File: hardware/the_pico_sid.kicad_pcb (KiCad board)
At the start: 4 copper layers, 26.7 x 56.5 mm, 22 parts, among them J2 Conn_01x05, Q1 2N7002, Q2 2N7002, U1 LM324, U2 SID_6581, U3 Pico, U4 4050, U5 4050, U6 74HC245

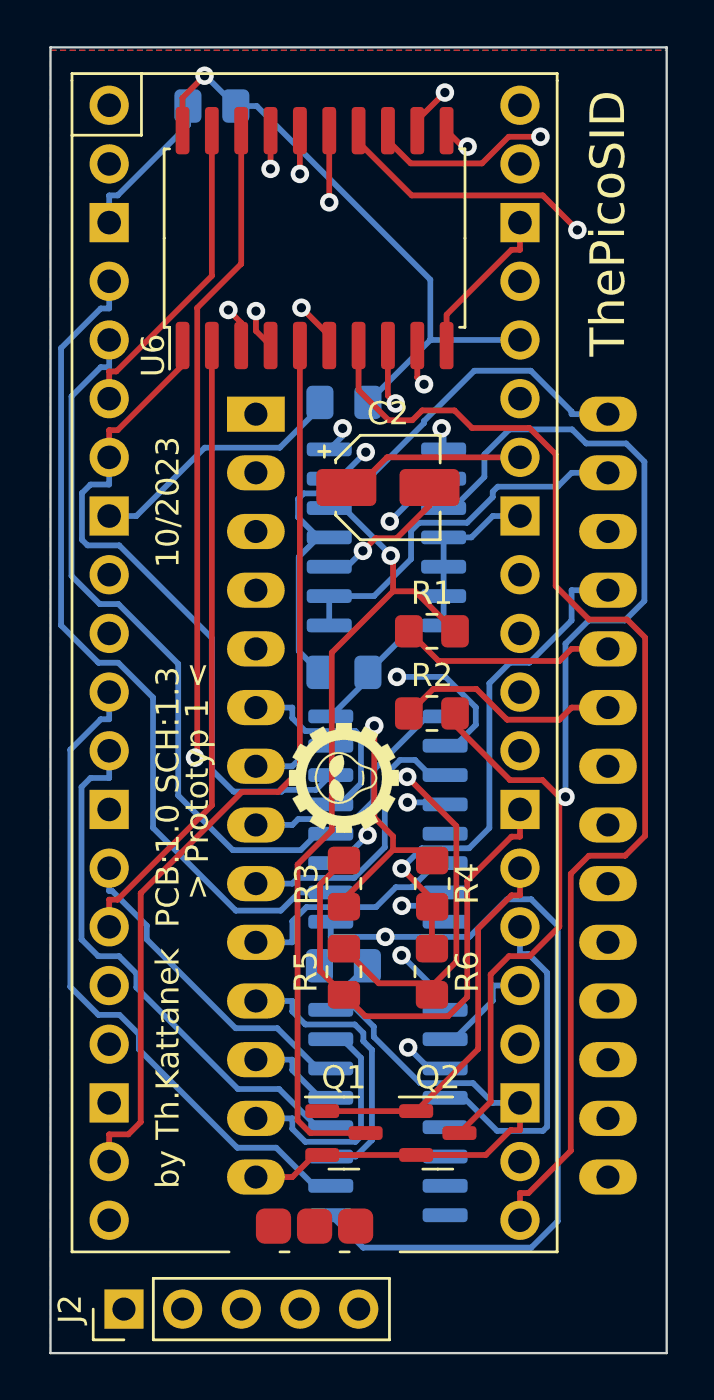
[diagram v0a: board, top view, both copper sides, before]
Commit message: schematic: change from 4050 to resistors for level convertion
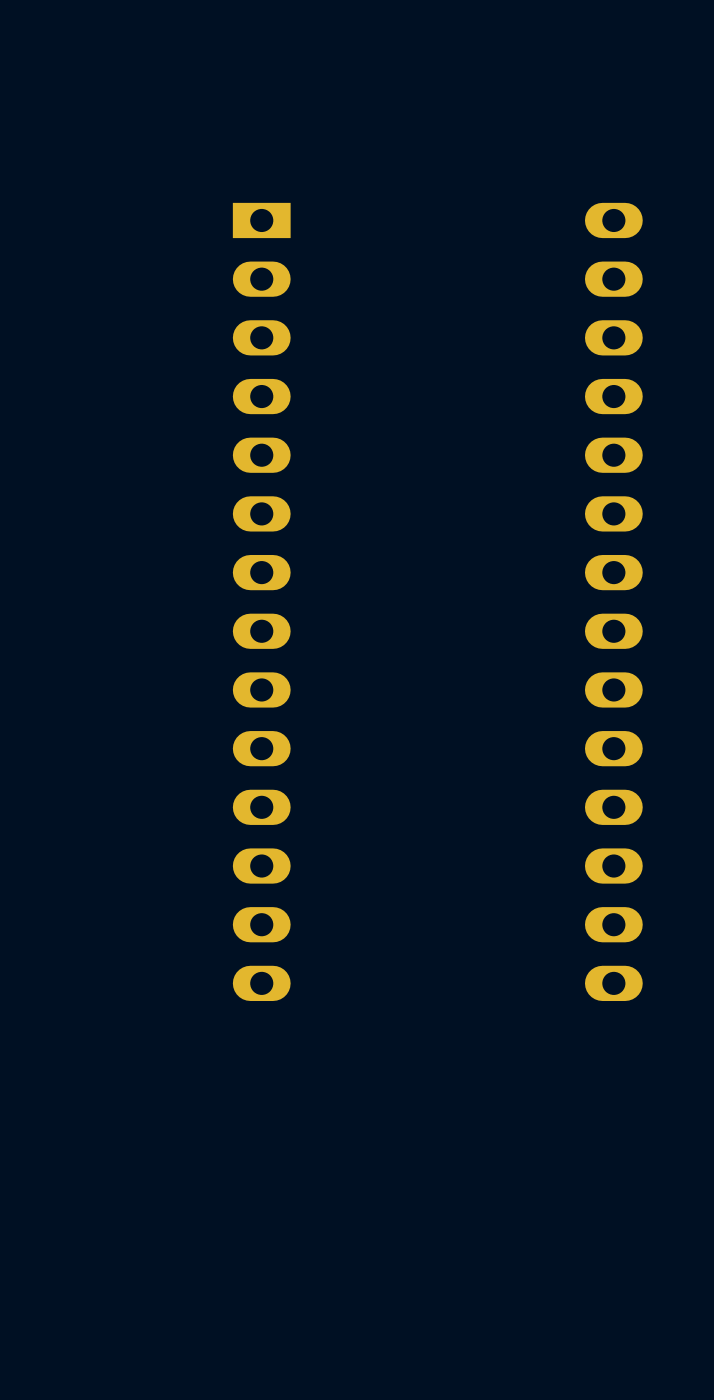
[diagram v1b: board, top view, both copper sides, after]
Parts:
- removed C1, C3, C4, C5: 100n, Capacitor_SMD:C_0805_2012Metric_Pad1.18x1.45mm_HandSolder
- removed C2: 1u, Capacitor_SMD:CP_Elec_4x4.5
- removed G***: LOGO, logos_tk:logo_01_4_8mm_fsilk
- removed J2: Conn_01x05, Connector_PinHeader_2.54mm:PinHeader_1x05_P2.54mm_Vertical
- removed Q1, Q2: 2N7002, Package_TO_SOT_SMD:SOT-23
- removed R1, R2: 1k, Resistor_SMD:R_0805_2012Metric_Pad1.20x1.40mm_HandSolder
- removed R3, R5: 56k, Resistor_SMD:R_0805_2012Metric_Pad1.20x1.40mm_HandSolder
- removed R4, R6: 150k, Resistor_SMD:R_0805_2012Metric_Pad1.20x1.40mm_HandSolder
- removed REF**: KiCad-Logo2_5mm_SilkScreen, Symbol:KiCad-Logo2_5mm_SilkScreen
- removed U1: LM324, Package_SO:SOIC-14_3.9x8.7mm_P1.27mm
- removed U3: Pico, connector_tk:RPi_Pico_SMD_TH
- removed U4, U5: 4050, Package_SO:SOIC-16_3.9x9.9mm_P1.27mm
- removed U6: 74HC245, Package_SO:SOIC-20W_7.5x12.8mm_P1.27mm
- moved U2 8.39 mm to (147.6, 97.0)
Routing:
- net GND: track 179.4 -> 0.00 mm
- net +3.3V: track 92.2 -> 0.00 mm, vias 2 -> 0
- net D0_C64: track 57.8 -> 0.00 mm, vias 1 -> 0
- net GPIO0: track 54.0 -> 0.00 mm
- net GPIO1: track 53.3 -> 0.00 mm
- net Net-(Q2-Pad3): track 51.5 -> 0.00 mm, vias 1 -> 0
- net D5: track 51.1 -> 0.00 mm
- net D1_C64: track 50.5 -> 0.00 mm, vias 1 -> 0
- net D4: track 49.9 -> 0.00 mm, vias 1 -> 0
- net D2_C64: track 47.1 -> 0.00 mm, vias 1 -> 0
- net D4_C64: track 45.2 -> 0.00 mm, vias 1 -> 0
- net D3_C64: track 44.1 -> 0.00 mm, vias 1 -> 0
- net +5V: track 43.8 -> 0.00 mm, vias 1 -> 0
- net D5_C64: track 42.7 -> 0.00 mm, vias 1 -> 0
- net GPIO22: track 42.0 -> 0.00 mm
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- removed copper zone on B.Cu, net GND
- removed copper zone on F.Cu, net GND
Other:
- board outline removed
- board text removed: "10/2023"
- board text removed: "> Prototyp 1 <"
- board text removed: "ThePicoSID"
- board text removed: "by Th.Kattanek PCB:1.0 SCH:1.3"

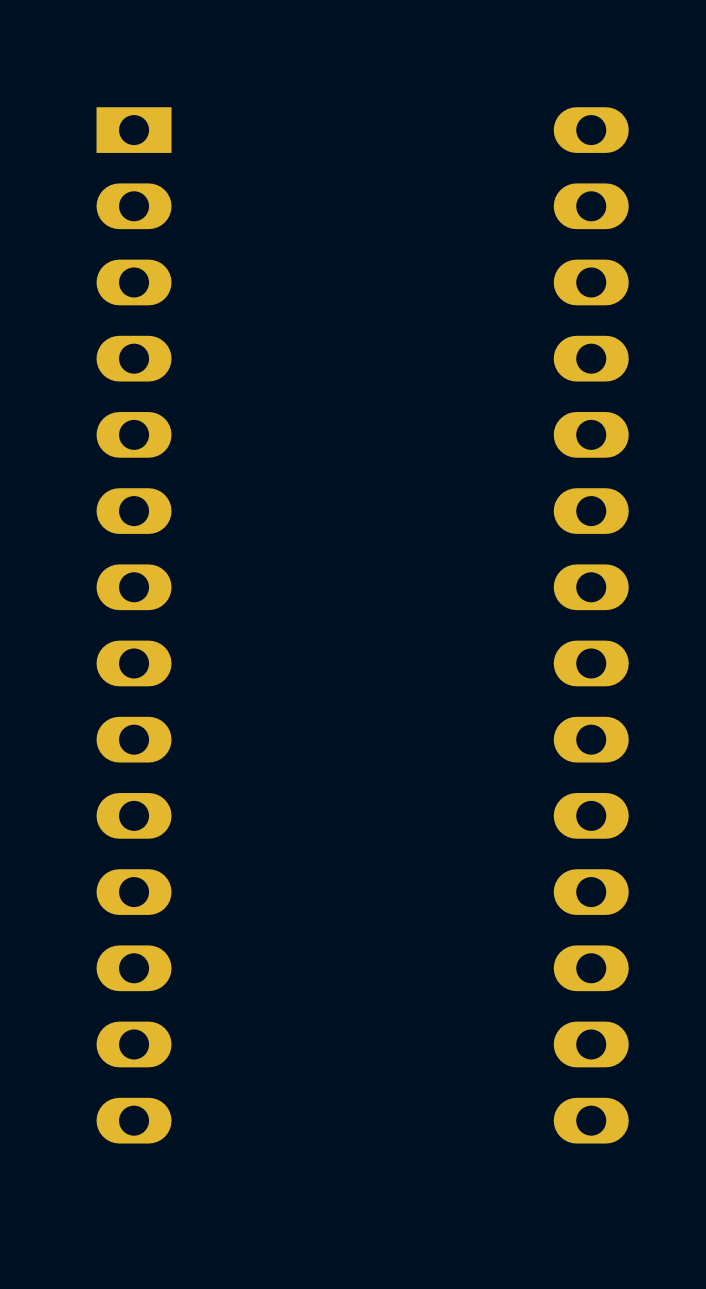
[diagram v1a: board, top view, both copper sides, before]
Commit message: pcb: first position all components in size from a sid
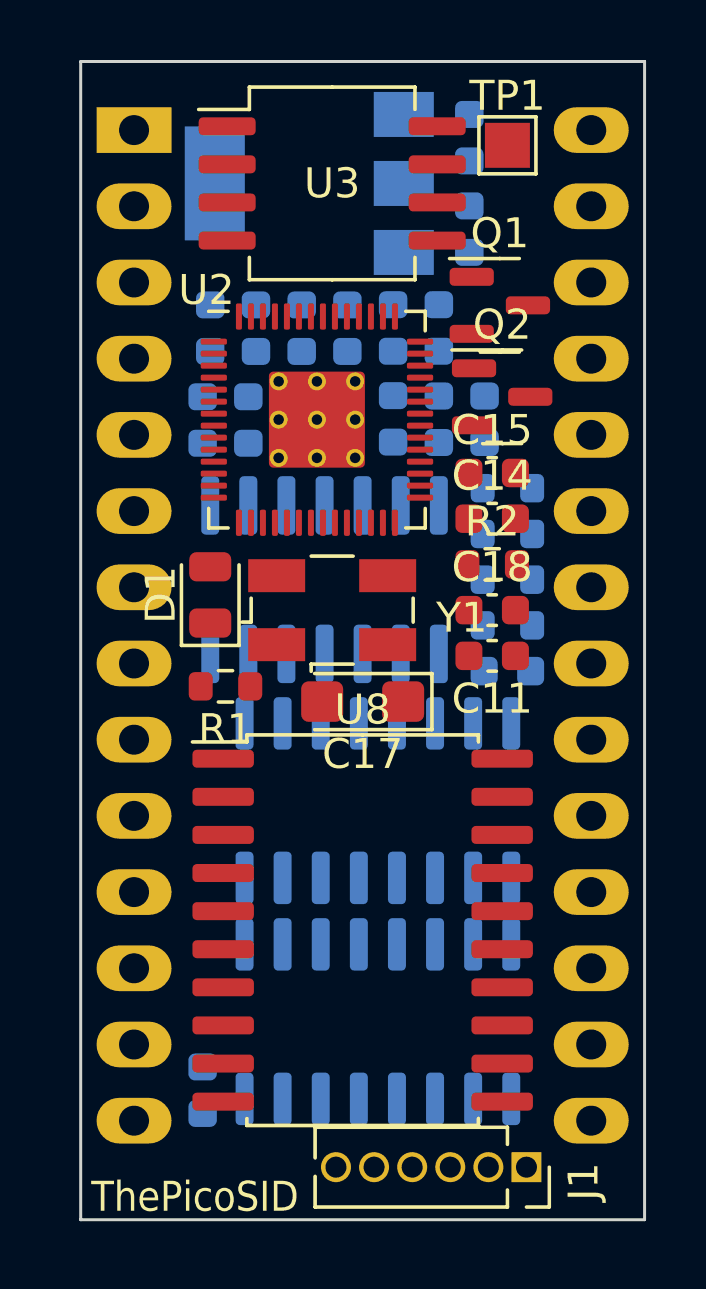
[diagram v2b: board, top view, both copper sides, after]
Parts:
- added C1: 100n, Capacitor_SMD:C_0603_1608Metric, B.Cu at (142.5, 87.1)
- added C10: 100n, Capacitor_SMD:C_0603_1608Metric, B.Cu at (151.6, 90.2)
- added C11: 100n, Capacitor_SMD:C_0603_1608Metric, F.Cu at (151.9, 98.0)
- added C12: 10u, Capacitor_SMD:C_0603_1608Metric, B.Cu at (151.1, 80.8)
- added C13: 10u, Capacitor_SMD:C_0603_1608Metric, B.Cu at (151.1, 83.8)
- added C14: 27p, Capacitor_SMD:C_0603_1608Metric, F.Cu at (151.9, 93.5)
- added C15: 27p, Capacitor_SMD:C_0603_1608Metric, F.Cu at (151.9, 91.9)
- added C16: 100n, Capacitor_SMD:C_0603_1608Metric, B.Cu at (148.6, 90.1)
- added C17: 1u, Capacitor_Tantalum_SMD:CP_EIA-3216-18_Kemet-A, F.Cu at (147.6, 99.6)
- added C18: 100n, Capacitor_SMD:C_0603_1608Metric, F.Cu at (151.9, 96.5)
- added C19: 100n, Capacitor_SMD:C_0603_1608Metric, B.Cu at (142.2, 112.5)
- added C2: 100n, Capacitor_SMD:C_0603_1608Metric, B.Cu at (150.1, 87.1)
- added C20: 100n, Capacitor_SMD:C_0603_1608Metric, B.Cu at (152.4, 98.6)
- added C3: 100n, Capacitor_SMD:C_0603_1608Metric, B.Cu at (148.6, 87.1)
- added C4: 100n, Capacitor_SMD:C_0603_1608Metric, B.Cu at (147.1, 87.1)
- added C5: 100n, Capacitor_SMD:C_0603_1608Metric, B.Cu at (145.5, 87.1)
- added C6: 100n, Capacitor_SMD:C_0603_1608Metric, B.Cu at (144.0, 87.1)
- added C7: 1u, Capacitor_SMD:C_0603_1608Metric, B.Cu at (142.2, 90.2)
- added C8: 1u, Capacitor_SMD:C_0603_1608Metric, B.Cu at (143.8, 90.2)
- added C9: 100n, Capacitor_SMD:C_0603_1608Metric, B.Cu at (150.1, 90.2)
- added D1: LED, LED_SMD:LED_0805_2012Metric, F.Cu at (142.5, 96.0)
- added J1: Conn_01x06, Connector_PinSocket_1.27mm:PinSocket_1x06_P1.27mm_Vertical, F.Cu at (153.0, 115.1)
- added Q1: 2N7002, Package_TO_SOT_SMD:SOT-23, F.Cu at (152.1, 86.4)
- added Q2: 2N7002, Package_TO_SOT_SMD:SOT-23, F.Cu at (152.2, 89.4)
- added R1: 470, Resistor_SMD:R_0603_1608Metric, F.Cu at (143.0, 99.1)
- added R2: 1k, Resistor_SMD:R_0603_1608Metric, F.Cu at (151.9, 95.0)
- added R3: 56k, Resistor_SMD:R_0603_1608Metric, B.Cu at (152.4, 94.0)
- added R4: 100k, Resistor_SMD:R_0603_1608Metric, B.Cu at (152.4, 92.5)
- added R5: 56k, Resistor_SMD:R_0603_1608Metric, B.Cu at (152.4, 95.5)
- added R6: 100k, Resistor_SMD:R_0603_1608Metric, B.Cu at (152.4, 97.0)
- added TP1: QSPI_SS, TestPoint:TestPoint_Pad_1.5x1.5mm, F.Cu at (152.4, 81.0)
- added U1: SID_6581, c64_tk:c64_sid_pins, B.Cu at (147.6, 97.0)
- added U3: W25Q16JVS, Package_SO:SO-8_5.3x6.2mm_P1.27mm, F.Cu at (146.6, 82.3)
- added U4: AMS1117-3.3, Package_TO_SOT_SMD:SOT-223-3_TabPin2, B.Cu at (145.8, 82.3)
- added U5: LM324, Package_SO:SOIC-14_3.9x8.7mm_P1.27mm, B.Cu at (146.3, 95.5)
- added U6: 4050, Package_SO:SO-16_3.9x9.9mm_P1.27mm, B.Cu at (148.1, 110.2)
- added U7: 4050, Package_SO:SO-16_3.9x9.9mm_P1.27mm, B.Cu at (148.1, 102.9)
- added U8: 74HC245, Package_SO:SOIC-20W_7.5x12.8mm_P1.27mm, F.Cu at (147.6, 107.2)
- added Y1: 12MHz, Crystal:Crystal_SMD_EuroQuartz_MJ-4Pin_5.0x3.2mm, F.Cu at (146.6, 96.5)
- U2: value SID_6581 -> RP2040; footprint c64_tk:c64_sid_pins -> MCU_RaspberryPi_and_Boards:RP2040-QFN-56; moved to F.Cu
- moved U2 7.03 mm to (146.1, 90.2), turned to 0 degrees
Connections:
- U2 pad 1: unconnected-(U2-Pad1) -> +3.3V
- U2 pad 10: A1_C64 -> +3.3V
- U2 pad 11: A2_C64 -> A2
- U2 pad 12: A3_C64 -> A3
- U2 pad 13: A4_C64 -> A4
- U2 pad 14: GND -> D0
- U2 pad 15: D0_C64 -> D1
- U2 pad 16: D1_C64 -> D2
- U2 pad 17: D2_C64 -> D3
- U2 pad 18: D3_C64 -> D4
- U2 pad 19: D4_C64 -> GND
- U2 pad 20: D5_C64 -> XIN
- U2 pad 21: D6_C64 -> XOUT
- U2 pad 22: D7_C64 -> +3.3V
- U2 pad 23: POTY -> +1V1
- U2 pad 24: POTX -> SWCLK
- U2 pad 25: +5V -> SWD
- U2 pad 27: AUDIO_OUT -> D5
- U2 pad 28: 9-12V -> D6
- U2 pad 4: unconnected-(U2-Pad4) -> RES
- U2 pad 5: RES_C64 -> CLK
- U2 pad 6: CLK_C64 -> CS
- U2 pad 7: RW_C64 -> RW
- U2 pad 8: CS_C64 -> A0
- U2 pad 9: A0_C64 -> A1
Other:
- board outline added: 18.8 x 38.6 mm
- board text added: "PCB:2.0 SCH:2.0"
- board text added: "ThePicoSID"

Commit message: convert to kicad 8.0
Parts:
- U2: footprint MCU_RaspberryPi_and_Boards:RP2040-QFN-56 -> Package_DFN_QFN:QFN-56-1EP_7x7mm_P0.4mm_EP3.2x3.2mm
- U6, U7: footprint Package_SO:SO-16_3.9x9.9mm_P1.27mm -> Package_SO:SOIC-16_3.9x9.9mm_P1.27mm
- moved U2 0.29 mm to (145.8, 90.0)
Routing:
- added copper zone on B.Cu, net GND
- added copper zone on F.Cu, net GND
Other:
- board text added: "by thorsten kattanek"

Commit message: schematic + pcb update
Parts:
- removed TP1: QSPI_SS, TestPoint:TestPoint_Pad_1.5x1.5mm
- added R2: 10k, Resistor_SMD:R_0603_1608Metric, F.Cu at (152.9, 82.0)
- C17: footprint Capacitor_Tantalum_SMD:CP_EIA-3216-18_Kemet-A -> Capacitor_SMD:C_0603_1608Metric
- renumbered C12 to C11, C13 to C12, C11 to C13, R2 to R3, R3 to R4, R4 to R5, R5 to R6, R6 to R7, U4 to U3, U3 to U4
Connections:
- C13 pad 1: Net-(U3-VCC) -> +3.3V
- J1 pad 1: GPIO22 -> GPIO00
- J1 pad 2: GPIO26 -> GPIO01
- J1 pad 3: GPIO27 -> GPIO22
- U2 pad 2: unconnected-(U2-GPIO0-Pad2) -> GPIO00
- U2 pad 3: unconnected-(U2-GPIO1-Pad3) -> GPIO01
- U2 pad 38: GPIO26 -> unconnected-(U2-GPIO26_ADC0-Pad38)
- U2 pad 39: GPIO27 -> unconnected-(U2-GPIO27_ADC1-Pad39)
- U4 pad 8: Net-(U3-VCC) -> +3.3V
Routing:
- net GND: track 0.00 -> 122.5 mm, vias 0 -> 4
- net +3.3V: track 0.00 -> 114.7 mm, vias 0 -> 3
- net GPIO01: track 0.00 -> 32.1 mm, vias 0 -> 1
- net GPIO00: track 0.00 -> 31.9 mm, vias 0 -> 1
- net RW: track 0.00 -> 30.1 mm, vias 0 -> 3
- net RES: track 0.00 -> 29.1 mm, vias 0 -> 2
- net CLK: track 0.00 -> 28.8 mm, vias 0 -> 2
- net CS: track 0.00 -> 28.6 mm, vias 0 -> 2
- net GPIO22: track 0.00 -> 26.9 mm, vias 0 -> 1
- net RES_C64: track 0.00 -> 26.2 mm, vias 0 -> 1
- net +5V: track 0.00 -> 25.5 mm, vias 0 -> 1
- net SWCLK: track 0.00 -> 22.8 mm, vias 0 -> 1
- net +1V1: track 0.00 -> 22.6 mm, vias 0 -> 3
- net CLK_C64: track 0.00 -> 22.6 mm, vias 0 -> 1
- net SWD: track 0.00 -> 22.3 mm, vias 0 -> 1
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- removed copper zone on B.Cu, net GND
- removed copper zone on F.Cu, net GND

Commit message: new gerber files for pcb 2.0
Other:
- board text added: "1"

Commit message: pcb: update
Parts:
- Q1, Q2, U8: moved to B.Cu
- U3, U5: moved to F.Cu
- moved R1 46.2 mm to (98.6, 86.1)
- moved C13 46.2 mm to (107.5, 85.1)
- moved C17 46.2 mm to (103.2, 86.6)
- moved C19 45.3 mm to (101.9, 92.0)
- moved C16 29.4 mm to (125.2, 72.4)
- moved C2 29.4 mm to (126.7, 69.3)
- moved C3 29.4 mm to (125.2, 69.3)
- moved C4 29.4 mm to (123.7, 69.3)
- moved C8 29.4 mm to (120.4, 72.4)
- moved C1 29.4 mm to (119.1, 69.3)
- moved C5 29.4 mm to (122.2, 69.3)
- moved C6 29.4 mm to (120.7, 69.3)
- moved C9 29.4 mm to (126.7, 72.4)
- moved C10 29.4 mm to (128.3, 72.4)
- moved C18 26.1 mm to (170.2, 78.0)
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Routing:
- net GND: track 122.5 -> 0.00 mm, vias 4 -> 0
- net +3.3V: track 114.7 -> 0.00 mm, vias 3 -> 0
- net GPIO01: track 32.1 -> 0.00 mm, vias 1 -> 0
- net GPIO00: track 31.9 -> 0.00 mm, vias 1 -> 0
- net RW: track 30.1 -> 0.00 mm, vias 3 -> 0
- net RES: track 29.1 -> 0.00 mm, vias 2 -> 0
- net CLK: track 28.8 -> 0.00 mm, vias 2 -> 0
- net CS: track 28.6 -> 0.00 mm, vias 2 -> 0
- net GPIO22: track 26.9 -> 0.00 mm, vias 1 -> 0
- net RES_C64: track 26.2 -> 0.00 mm, vias 1 -> 0
- net +5V: track 25.5 -> 0.00 mm, vias 1 -> 0
- net SWCLK: track 22.8 -> 0.00 mm, vias 1 -> 0
- net +1V1: track 22.6 -> 0.00 mm, vias 3 -> 0
- net CLK_C64: track 22.6 -> 0.00 mm, vias 1 -> 0
- net SWD: track 22.3 -> 0.00 mm, vias 1 -> 0
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
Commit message: new pcb and gerber files for JLCPCB production
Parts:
- C1, C10, C11, C12, C16, C19, C2, C3, C4, C5, C6, C7, C8, C9, R4, R5, R6, R7: moved to F.Cu
- C18: moved to B.Cu
- moved C6 52.4 mm to (152.5, 110.9), turned to 0 degrees
- moved C17 50.0 mm to (153.2, 87.0), turned to 90 degrees
- moved C5 48.0 mm to (152.5, 106.6), turned to 0 degrees
- moved C13 47.1 mm to (153.3, 96.3), turned to 90 degrees
- moved R1 46.7 mm to (142.8, 101.2)
- moved C1 46.3 mm to (152.5, 101.5), turned to 0 degrees
- moved C4 46.1 mm to (152.5, 105.3), turned to 0 degrees
- moved C10 44.2 mm to (152.5, 109.3), turned to 0 degrees
- moved C3 44.1 mm to (152.5, 104.0), turned to 0 degrees
- moved C9 43.8 mm to (152.5, 107.8), turned to 0 degrees
- moved C2 42.2 mm to (152.5, 102.7), turned to 0 degrees
- moved C19 40.5 mm to (142.4, 92.6)
- moved C18 40.0 mm to (152.1, 113.7)
- moved C8 37.7 mm to (142.1, 103.3), turned to 90 degrees
- moved C20 32.3 mm to (142.4, 85.9), turned to 90 degrees
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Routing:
- net GND: track 0.00 -> 139.6 mm, vias 0 -> 3
- net +3.3V: track 0.00 -> 112.8 mm, vias 0 -> 3
- net RW: track 0.00 -> 39.8 mm, vias 0 -> 1
- net A4_C64: track 0.00 -> 33.9 mm, vias 0 -> 1
- net A3: track 0.00 -> 31.6 mm, vias 0 -> 2
- net +5V: track 0.00 -> 28.1 mm
- net A3_C64: track 0.00 -> 27.4 mm, vias 0 -> 1
- net A2: track 0.00 -> 27.2 mm, vias 0 -> 2
- net ADC_2KHZ: track 0.00 -> 26.5 mm, vias 0 -> 2
- net A4: track 0.00 -> 26.3 mm, vias 0 -> 2
- net POTY: track 0.00 -> 26.0 mm, vias 0 -> 1
- net A2_C64: track 0.00 -> 23.1 mm, vias 0 -> 1
- net POTX: track 0.00 -> 20.8 mm
- net AUDIO_PWM: track 0.00 -> 20.0 mm, vias 0 -> 2
- net CS: track 0.00 -> 20.0 mm, vias 0 -> 1
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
